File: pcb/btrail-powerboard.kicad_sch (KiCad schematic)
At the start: 13 parts, among them J1 RJ45_Shielded, Q1 IRLZ34N, Q2 IRLZ34N

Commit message: Final revision, added ground plane and more compact design, thanks Emily!
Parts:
- 24V_In1, Motor1: footprint Connector_PinHeader_1.00mm:PinHeader_1x02_P1.00mm_Vertical -> Connector_PinHeader_2.54mm:PinHeader_1x02_P2.54mm_Vertical
- 5V+1, GND1, GND2, Vin_DC-DC1: footprint Connector_PinSocket_1.00mm:PinSocket_1x02_P1.00mm_Vertical -> Connector_PinSocket_2.54mm:PinSocket_1x02_P2.54mm_Vertical
- DRV8874_left1, DRV8874_right1: footprint Connector_PinHeader_1.00mm:PinHeader_1x06_P1.00mm_Vertical -> Connector_PinHeader_2.54mm:PinHeader_1x06_P2.54mm_Vertical
- ESP32_jack1: footprint Connector_PinHeader_1.00mm:PinHeader_1x09_P1.00mm_Vertical -> Connector_PinHeader_2.54mm:PinHeader_1x09_P2.54mm_Vertical
- LED1/LED2: footprint Connector_PinHeader_1.00mm:PinHeader_1x04_P1.00mm_Vertical -> Connector_PinHeader_2.54mm:PinHeader_1x04_P2.54mm_Vertical
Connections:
- net +24V: now reaches 24V_In1.2 (Pin_2), DRV8874_right1.1 (Pin_1), J1.1, J1.8, Q1.3 (S), Q2.3 (S), Vin_DC-DC1.1 (Pin_1), Vin_DC-DC1.2 (Pin_2)
- net GND: now reaches 24V_In1.1 (Pin_1), DRV8874_left1.2 (Pin_2), DRV8874_right1.2 (Pin_2), DRV8874_right1.6 (Pin_6), ESP32_jack1.9 (Pin_9), GND1.1 (Pin_1), GND1.2 (Pin_2), GND2.1 (Pin_1), GND2.2 (Pin_2), J1.2, J1.7, LED1/LED2.2 (Pin_2), LED1/LED2.4 (Pin_4)
- net +5V: now reaches 5V+1.1 (Pin_1), 5V+1.2 (Pin_2), DRV8874_left1.5 (Pin_5), DRV8874_left1.6 (Pin_6), ESP32_jack1.8 (Pin_8)

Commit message: Sync for coop purposes
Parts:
- Q1, Q2: value IRLZ34N -> IRL540NPBF
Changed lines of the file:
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@@
 	)
 	(junction
-		(at 33.02 92.71)
+		(at 39.37 92.71)
 		(diameter 0)
 		(color 0 0 0 0)
@@
 	(wire
 		(pts
-			(xy 33.02 90.17) (xy 38.1 90.17)
+			(xy 39.37 90.17) (xy 38.1 90.17)
 		)
 		(stroke
@@
 			(width 0)
 			(type default)
-		)
-	)
-	(wire
-		(pts
-			(xy 33.02 92.71) (xy 33.02 90.17)
+			(color 255 0 17 1)
+		)
+	)
+	(wire
+		(pts
+			(xy 39.37 92.71) (xy 39.37 90.17)
 		)
 		(stroke
@@
 	(wire
 		(pts
-			(xy 33.02 181.61) (xy 33.02 92.71)
+			(xy 39.37 181.61) (xy 39.37 92.71)
 		)
 		(stroke
@@
 	(wire
 		(pts
-			(xy 66.04 181.61) (xy 33.02 181.61)
+			(xy 66.04 181.61) (xy 39.37 181.61)
 		)
 		(stroke
@@
 	(wire
 		(pts
-			(xy 33.02 92.71) (xy 38.1 92.71)
+			(xy 39.37 92.71) (xy 38.1 92.71)
 		)
 		(stroke
@@
 			(width 0)
 			(type default)
+			(color 255 0 17 1)
 		)
 	)
@@
 			(width 0)
 			(type default)
+			(color 255 0 11 1)
 		)
 	)
@@
 		(on_board yes)
 		(dnp no)
-		(fields_autoplaced yes)
 		(property "Reference" "DRV8874_right1"
-			(at 43.815 74.93 0)
+			(at 48.768 74.93 0)
 			(effects
 				(font
@@
 		)
 		(property "Value" "Conn_01x06_Pin"
-			(at 43.815 77.47 0)
+			(at 49.022 77.47 0)
 			(effects
 				(font
@@
 			)
 		)
-		(property "Value" "IRLZ34N"
+		(property "Value" "IRL540NPBF"
 			(at 135.89 77.4699 0)
 			(effects
@@
 		(on_board yes)
 		(dnp no)
-		(fields_autoplaced yes)
 		(property "Reference" "DRV8874_left1"
-			(at 33.655 74.93 0)
+			(at 29.464 74.93 0)
 			(effects
 				(font
@@
 		)
 		(property "Value" "Conn_01x06_Pin"
-			(at 33.655 77.47 0)
+			(at 28.194 77.47 0)
 			(effects
 				(font
@@
 		(dnp no)
 		(property "Reference" "5V+1"
-			(at 150.368 170.434 0)
+			(at 150.876 168.91 0)
 			(effects
 				(font
@@
 		(on_board yes)
 		(dnp no)
-		(fields_autoplaced yes)
 		(property "Reference" "Q2"
-			(at 130.81 60.9599 0)
+			(at 135.636 60.706 0)
 			(effects
 				(font
@@
 			)
 		)
-		(property "Value" "IRLZ34N"
-			(at 130.81 63.4999 0)
-			(effects
-				(font
+		(property "Value" "IRL540NPBF"
+			(at 135.636 63.5 0)
+			(effects
+				(font

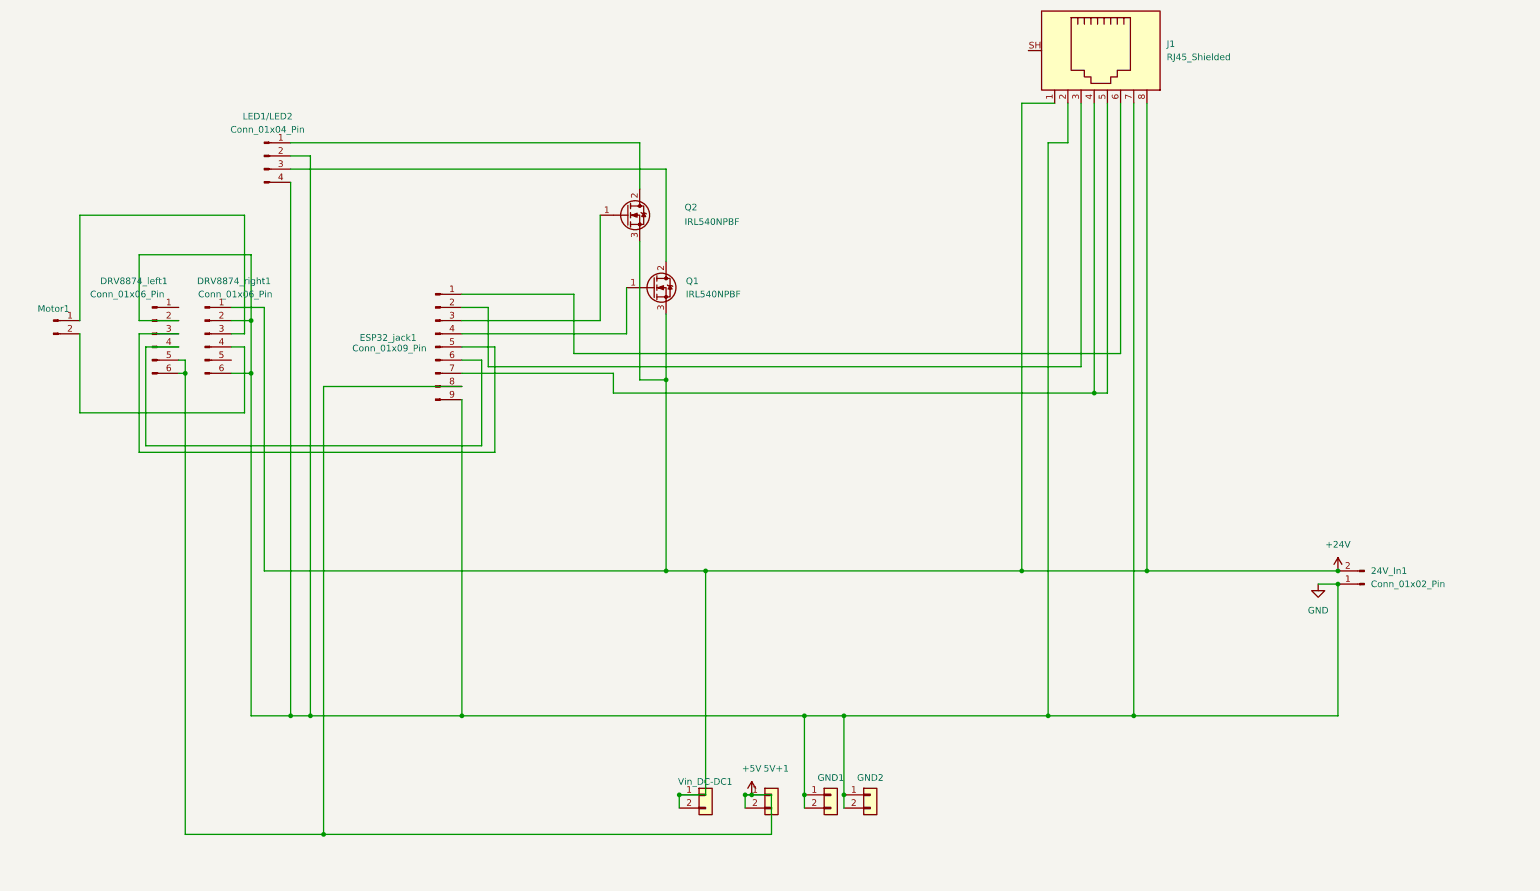
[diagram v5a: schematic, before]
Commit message: New board revision: Add full wave rectifier
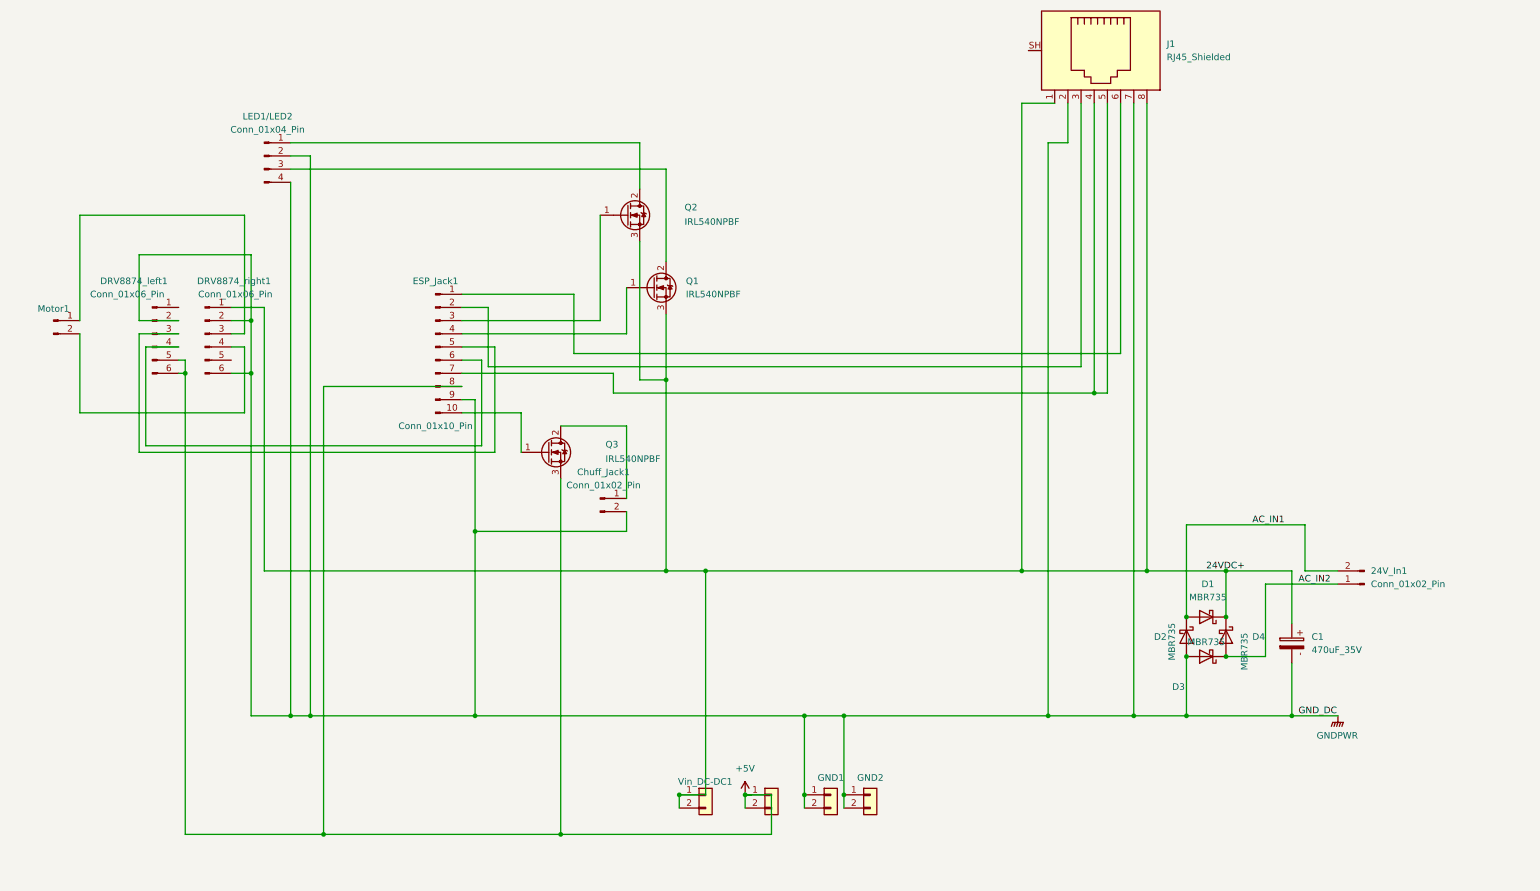
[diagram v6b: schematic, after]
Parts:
- added C1: 470uF_35V, Capacitor_THT:CP_Radial_D10.0mm_P5.00mm, symbol PCM_SL_Capacitors:470uF_35V
- added Chuff_Jack1: Conn_01x02_Pin, Connector_PinHeader_2.54mm:PinHeader_1x02_P2.54mm_Vertical, symbol Connector:Conn_01x02_Pin
- added D1, D2, D3, D4: MBR735, Package_TO_SOT_THT:TO-220-2_Vertical, symbol Diode:MBR735
- added Q3: IRL540NPBF, Package_TO_SOT_THT:TO-220-3_Vertical, symbol Transistor_FET:IRLZ34N
- ESP_Jack1: renamed from ESP32_jack1; value Conn_01x09_Pin -> Conn_01x10_Pin; footprint Connector_PinHeader_2.54mm:PinHeader_1x09_P2.54mm_Vertical -> Connector_PinHeader_2.54mm:PinHeader_1x10_P2.54mm_Vertical; symbol Connector:Conn_01x09_Pin -> Connector:Conn_01x10_Pin
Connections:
- net +5V: now also Q3.3 (S)
- net +24V renamed 24VDC+
- net 24VDC+: now also C1.1, D1.1 (K), D4.1 (K); no longer 24V_In1.2 (Pin_2)
- net GND renamed GNDPWR
- net GNDPWR: now also C1.2, Chuff_Jack1.2 (Pin_2), D2.2 (A), D3.2 (A); no longer 24V_In1.1 (Pin_1)
- new net: Chuff_Jack1.1 (Pin_1), Q3.2 (D)
- new net: ESP_Jack1.10 (Pin_10), Q3.1 (G)
- new net AC_IN1: 24V_In1.2 (Pin_2), D1.2 (A), D2.1 (K)
- new net AC_IN2: 24V_In1.1 (Pin_1), D3.1 (K), D4.2 (A)

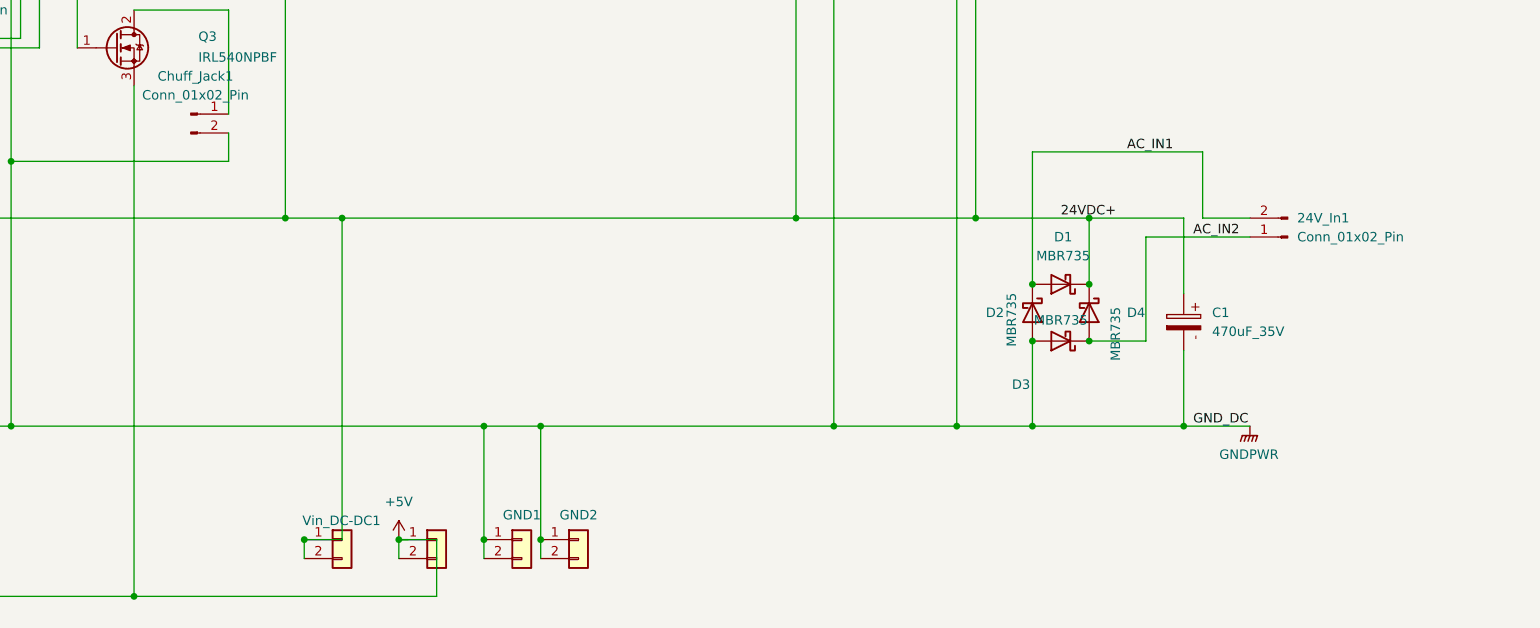
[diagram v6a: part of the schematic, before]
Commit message: Update PCB to latest full bridge rectifier version
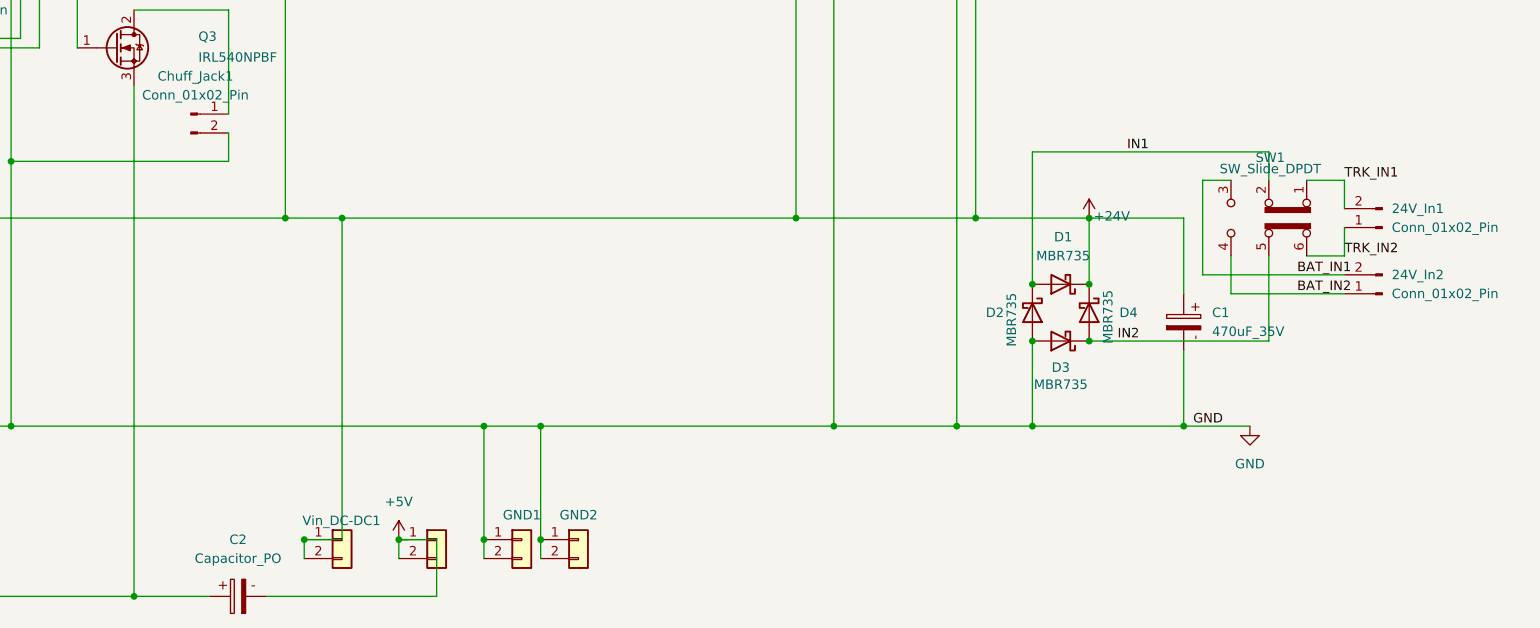
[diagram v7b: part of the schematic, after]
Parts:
- added 24V_In2: Conn_01x02_Pin, Connector_PinHeader_2.54mm:PinHeader_1x02_P2.54mm_Vertical, symbol Connector:Conn_01x02_Pin
- added C2: Capacitor_PO, Capacitor_THT:CP_Radial_D5.0mm_P2.50mm, symbol PCM_SL_Devices:Capacitor_PO
- added SW1: SW_Slide_DPDT, Button_Switch_THT:SW_NKK_G1xJP, symbol Switch:SW_Slide_DPDT
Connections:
- net +5V: now also C2.2; no longer DRV8874_left1.5 (Pin_5), DRV8874_left1.6 (Pin_6), ESP_Jack1.8 (Pin_8), Q3.3 (S)
- net 24VDC+ renamed +24V
- net AC_IN1 renamed IN1
- net IN1: now also SW1.2 (B); no longer 24V_In1.2 (Pin_2)
- net AC_IN2 renamed IN2
- net IN2: now also SW1.5 (B); no longer 24V_In1.1 (Pin_1)
- net GNDPWR renamed GND
- new net: C2.1, DRV8874_left1.5 (Pin_5), DRV8874_left1.6 (Pin_6), ESP_Jack1.8 (Pin_8), Q3.3 (S)
- new net BAT_IN1: 24V_In2.2 (Pin_2), SW1.3 (C)
- new net BAT_IN2: 24V_In2.1 (Pin_1), SW1.4 (A)
- new net TRK_IN1: 24V_In1.2 (Pin_2), SW1.1 (A)
- new net TRK_IN2: 24V_In1.1 (Pin_1), SW1.6 (C)
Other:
- moved on the sheet: 24V_In1
